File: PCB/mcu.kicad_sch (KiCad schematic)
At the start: 35 parts, among them J1 USB_C_Receptacle_USB2.0, SW105 RotaryEncoder, SW106 SW_DIP_x01, SW107 SW_DIP_x01, SW108 SW_DIP_x01, U14 TLV1117LV, U15 ATSAM4S4BA-AU, Y1 XTAL-12M

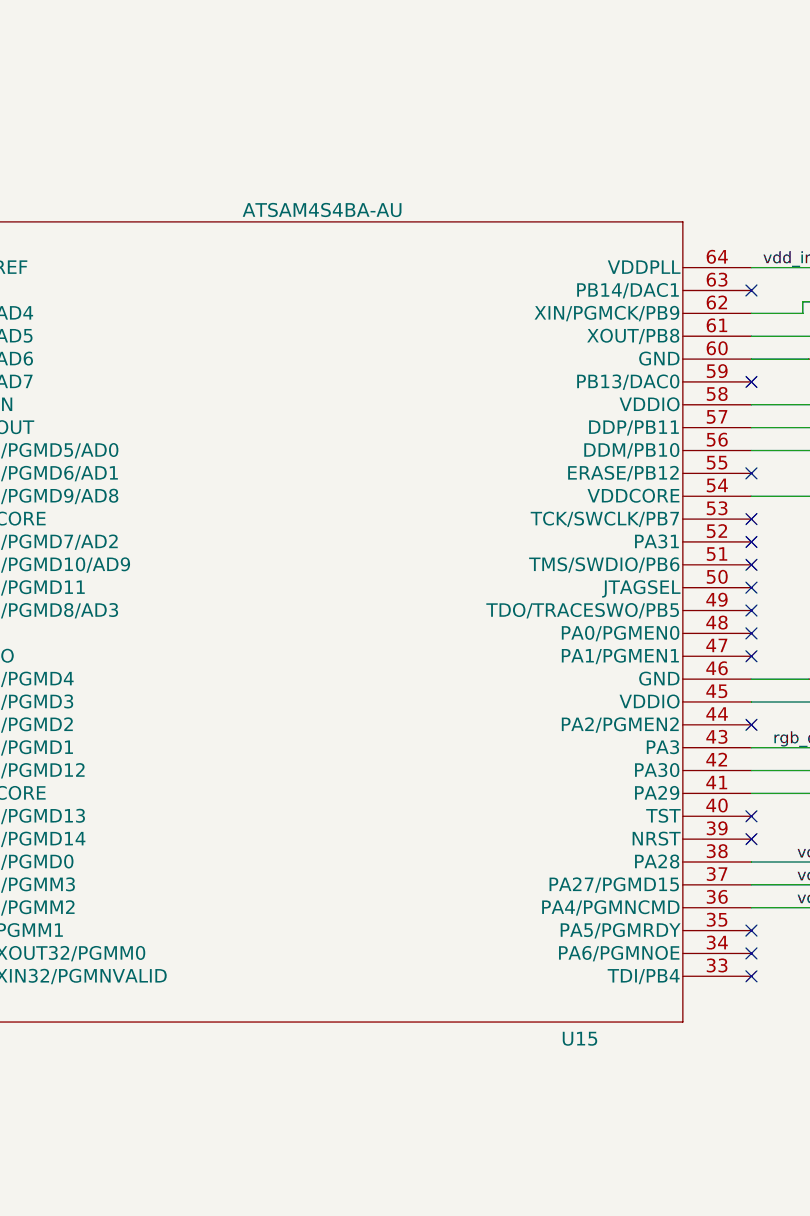
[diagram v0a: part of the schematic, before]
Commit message: FreeRTOS blink example working
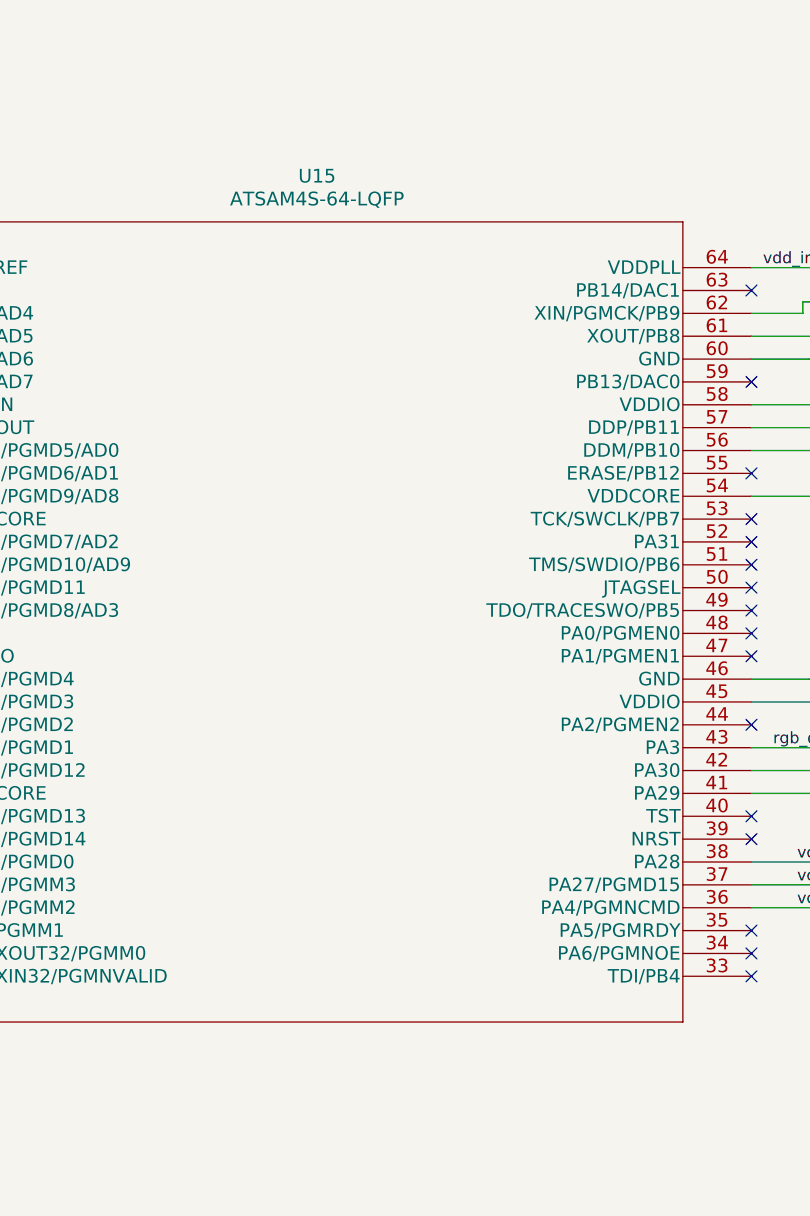
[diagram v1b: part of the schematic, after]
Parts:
- U15: value ATSAM4S4BA-AU -> ATSAM4S-64-LQFP; footprint Package_QFP:TQFP-64_10x10mm_P0.5mm -> QFP64-10x10MC_MCH; symbol SAM4_User:ATSAM4S4BA-AU -> SAM4_User:ATSAM4S-64-LQFP
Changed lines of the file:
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@@
     (pin "2")
   )
-  (symbol (lib_id "SAM4_User:ATSAM4S4BA-AU") (at 53.34 46.355 0) (unit 1)
+  (symbol (lib_id "SAM4_User:ATSAM4S-64-LQFP") (at 53.34 46.355 0) (unit 1)
     (in_bom yes) (on_board yes)
-    (property "Reference" "U15" (id 0) (at 130.81 132.08 0)
+    (property "Reference" "U15" (id 0) (at 101.6 36.195 0)
       (effects (font (size 1.524 1.524)))
     )
-    (property "Value" "ATSAM4S4BA-AU" (id 1) (at 102.235 40.005 0)
+    (property "Value" "ATSAM4S-64-LQFP" (id 1) (at 101.6 38.735 0)
       (effects (font (size 1.524 1.524)))
     )
-    (property "Footprint" "Package_QFP:TQFP-64_10x10mm_P0.5mm" (id 2) (at 101.6 40.259 0)
+    (property "Footprint" "QFP64-10x10MC_MCH" (id 2) (at 101.6 40.259 0)
       (effects (font (size 1.524 1.524)) hide)
     )
